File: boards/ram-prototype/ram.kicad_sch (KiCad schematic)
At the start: 48 parts, among them J1 SRAM_Bus, J2 DEC3_Unused, J3 Unused_COL_SEL, J4 DEC4_Unused

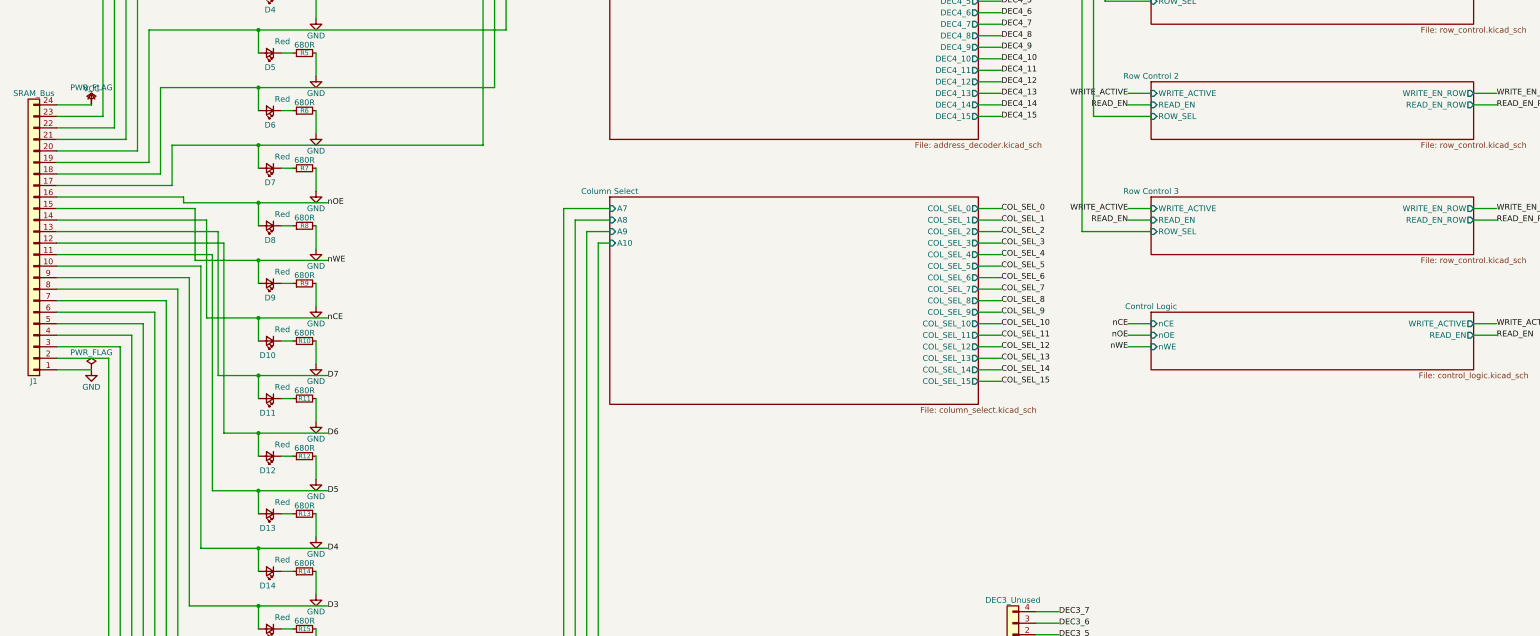
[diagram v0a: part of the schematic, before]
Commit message: add 8-pin PCIe power connector + TPS546D24A buck converter circuit
Adds on-board 12V→3.3V power supply to the RAM prototype using a
TPS546D24A 40A synchronous buck converter fed by an 8-pin PCIe
(Molex Mini-Fit Jr 2x4) connector. This establishes the power
architecture for all future boards (CPU, PPU).

New files:
- power_supply.kicad_sch: PCIe connector, buck converter, input/output
  filter caps, bootstrap/bypass caps, EN divider, PGOOD LED indicator
- shared/kicad-lib/symbols/Power_Discrete.kicad_sym: custom TPS546D24A
  symbol (41 pins at unique positions, placeholder footprint)

Infrastructure:
- symbols.py loads custom libs via CUSTOM_SYMBOL_LIBS in common.py
- schematic.py gains add_no_connect() and add_text() methods
- verify.py filters lib_symbol_issues as standalone artifact
- Library tables updated for Connector_Molex, Inductor_SMD, etc.

0 ERC errors, 0 verification warnings. 618 total BOM parts (+7).

Co-Authored-By: Claude Opus 4.6 (1M context) <noreply@anthropic.com>
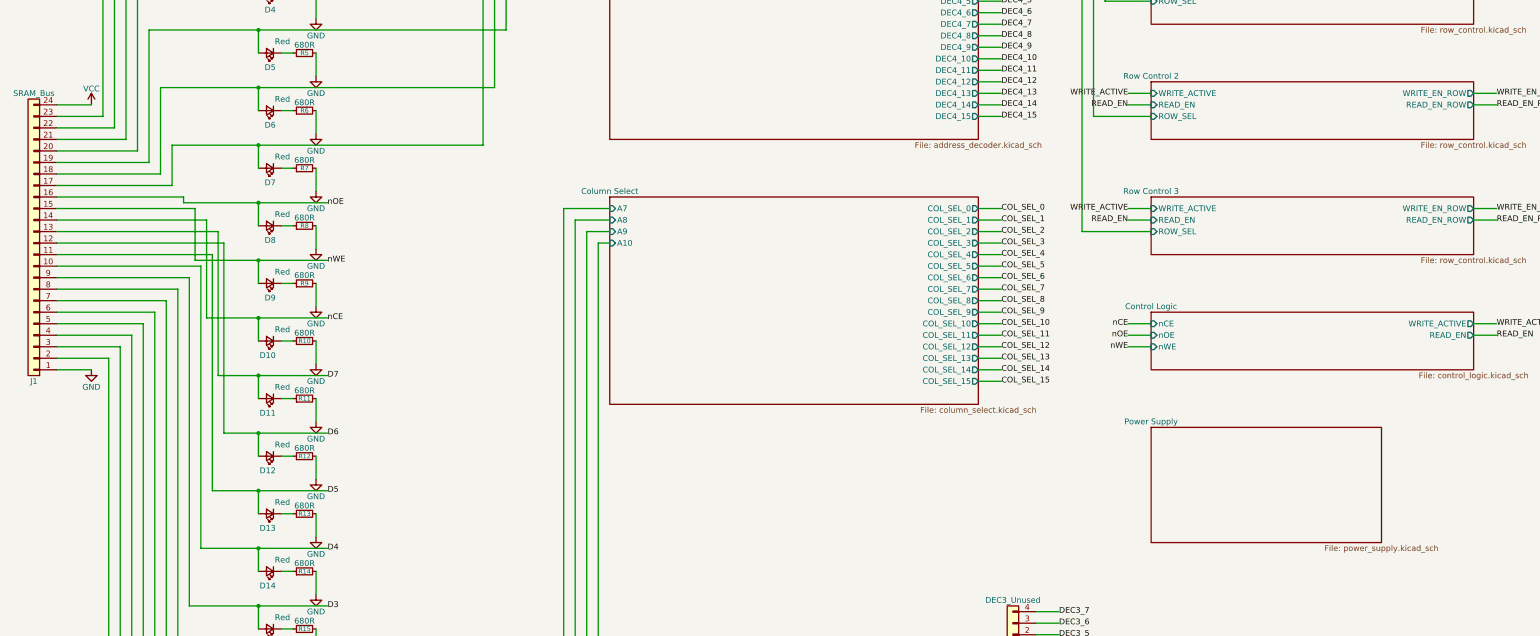
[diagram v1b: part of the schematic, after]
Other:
- added sheet Power Supply (power_supply.kicad_sch)

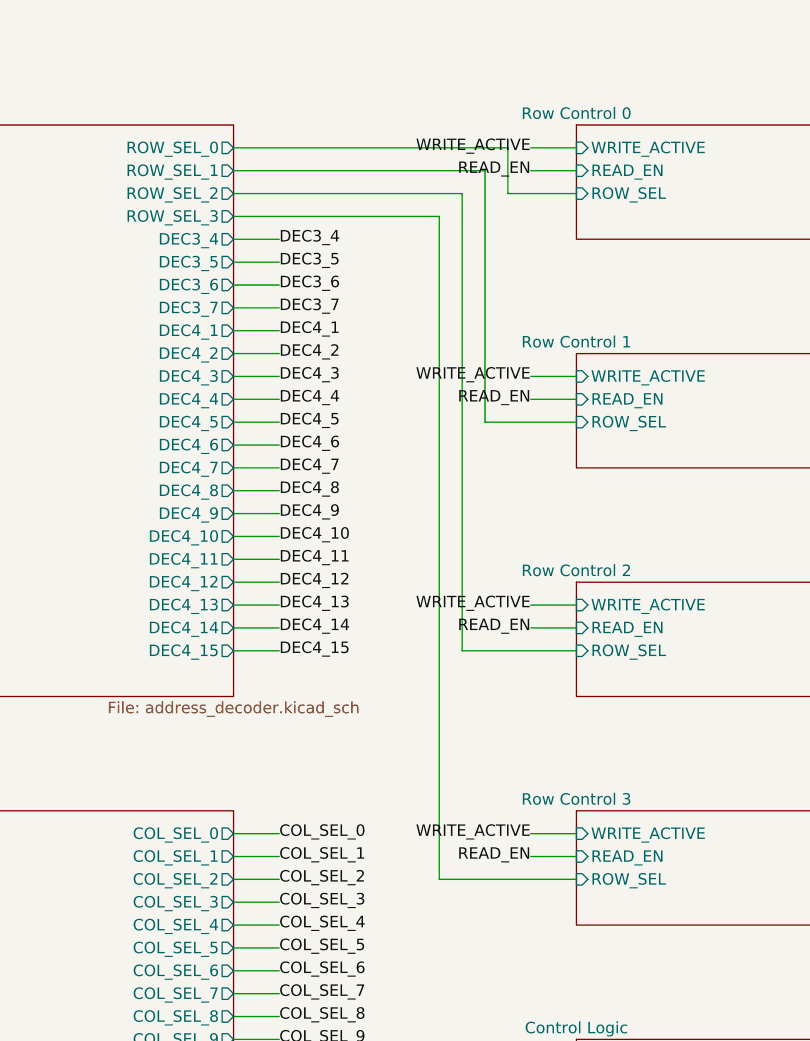
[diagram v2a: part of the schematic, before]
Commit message: add text overlap check to schematic verification and fix all violations
New check #12 in verify.py detects text overlapping wires, component
bodies, or other text. Smart exclusions for labels on their connection
wire and same-component Reference/Value pairs avoid false positives.

Fixes in generate_ram.py:
- Move ROW_SEL trunk wires from col2_x-3*GRID to col2_x-7*GRID so
  WRITE_ACTIVE/READ_EN labels don't overlap them
- Power supply: switch VDD5/BP1V5 bypass caps to angle=0 (vertical)
  with L-routes and 4*GRID vertical drop from IC pins
- Power supply: separate PGD L-route vertical X from pull-up resistor X
- Power supply: hide boot cap value (pin 2 wire unavoidably crosses it)

Co-Authored-By: Claude Opus 4.6 (1M context) <noreply@anthropic.com>
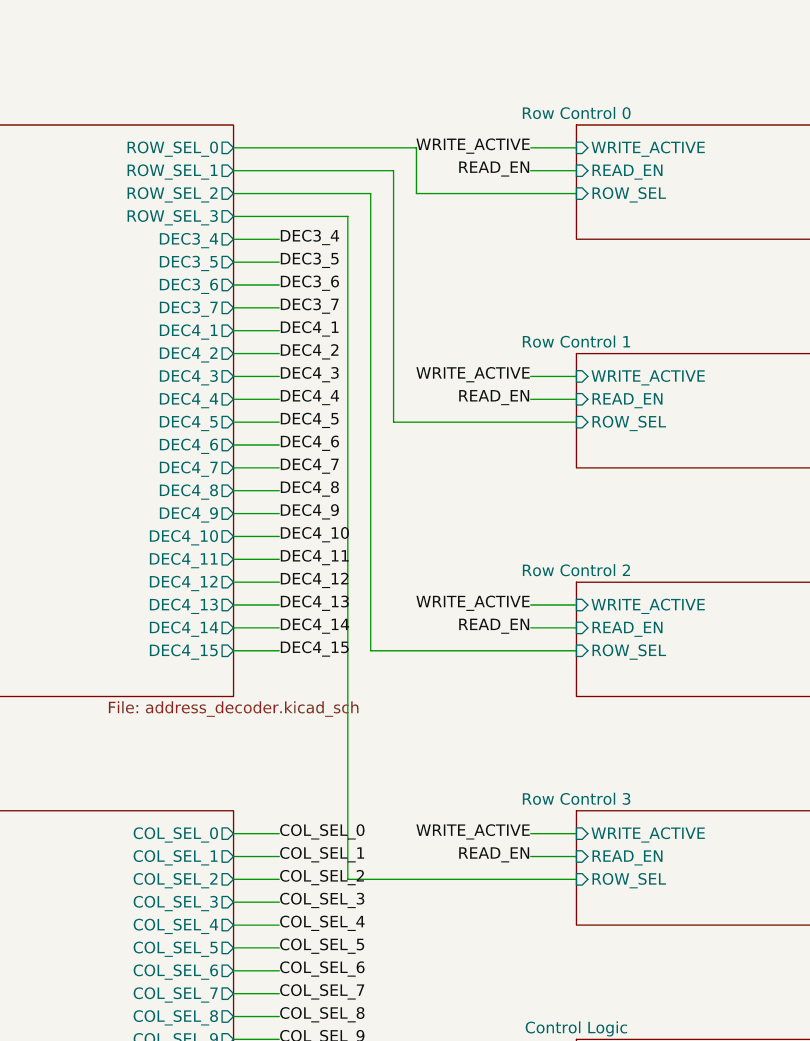
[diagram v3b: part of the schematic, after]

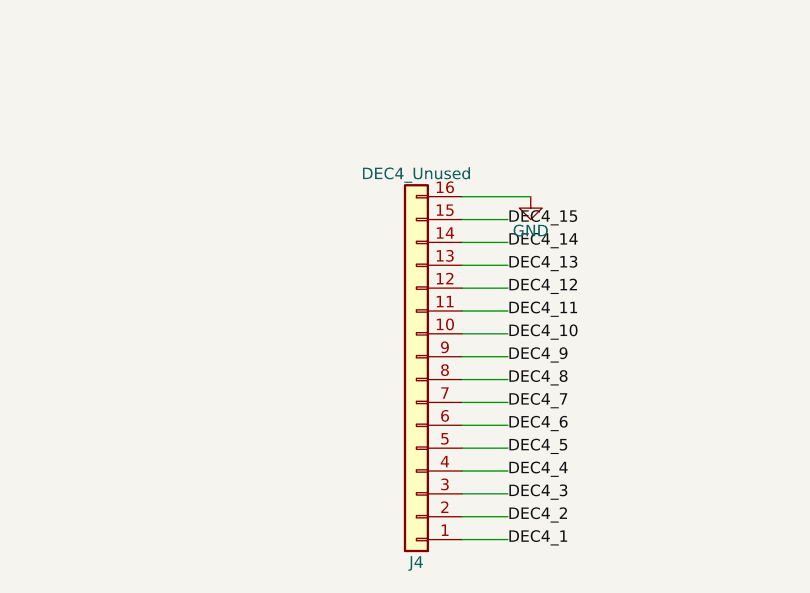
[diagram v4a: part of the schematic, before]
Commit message: replace J4 with 2-row connector and reposition J2/J4 headers
- Change J4 (DEC4 unused outputs) from Conn_01x16 to Conn_02x08_Odd_Even
  (2-row vertical pin header, more compact than 16-pin single row)
- Move J2 (DEC3) to top-left corner above main connector
- Move J4 (DEC4) to left of test grid, vertical orientation
- Add Conn_02x08_Odd_Even to symbol/footprint library maps
- Board size: 173 x 118 mm (down from 233 x 95 mm)
- 0 ERC errors/warnings, 0 DRC errors/warnings

Co-Authored-By: Claude Opus 4.6 (1M context) <noreply@anthropic.com>
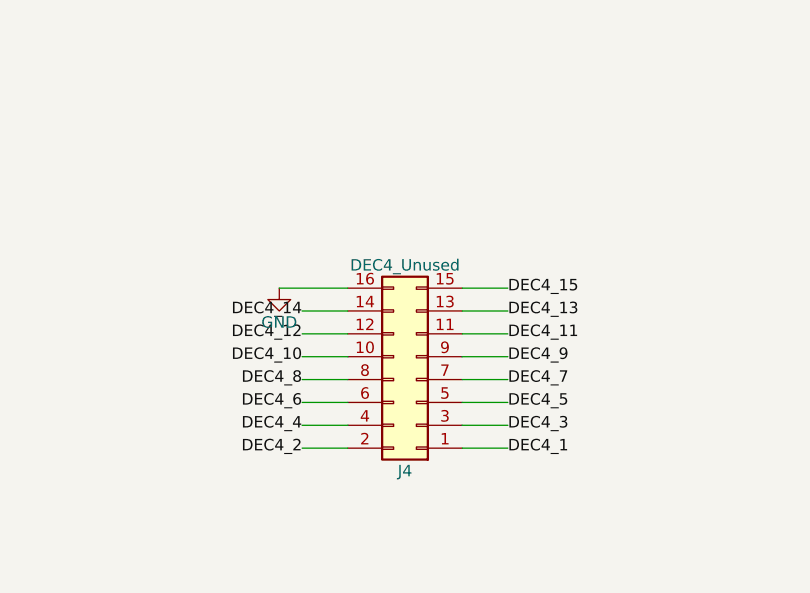
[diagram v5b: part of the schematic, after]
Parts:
- removed J4: DEC4_Unused, symbol Connector_Generic:Conn_01x16
- added J4: DEC4_Unused, symbol Connector_Generic:Conn_02x08_Odd_Even
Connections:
- net DEC4_1: now also J4.1 (Pin_1)
- net DEC4_10: now also J4.10 (Pin_10)
- net DEC4_11: now also J4.11 (Pin_11)
- net DEC4_12: now also J4.12 (Pin_12)
- net DEC4_13: now also J4.13 (Pin_13)
- net DEC4_14: now also J4.14 (Pin_14)
- net DEC4_15: now also J4.15 (Pin_15)
- net DEC4_2: now also J4.2 (Pin_2)
- net DEC4_3: now also J4.3 (Pin_3)
- net DEC4_4: now also J4.4 (Pin_4)
- net DEC4_5: now also J4.5 (Pin_5)
- net DEC4_6: now also J4.6 (Pin_6)
- net DEC4_7: now also J4.7 (Pin_7)
- net DEC4_8: now also J4.8 (Pin_8)
- net DEC4_9: now also J4.9 (Pin_9)
- net GND: now also J4.16 (Pin_16)

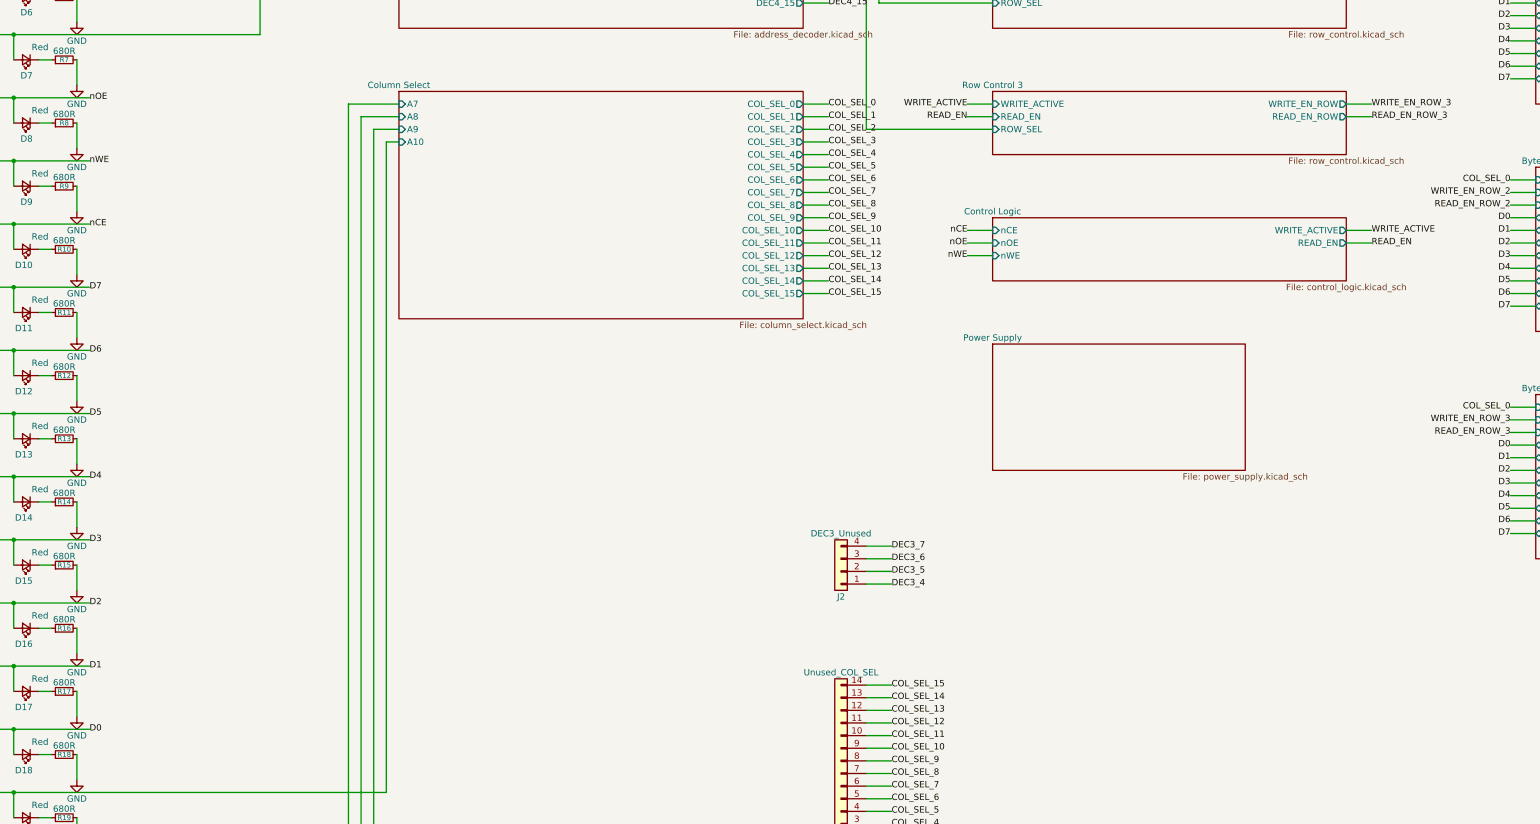
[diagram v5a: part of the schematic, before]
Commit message: swap D* and ctrl pins on connector, move ctrl logic below power supply
Data bus (D0-D7) now at pins 9-16, control (nCE/nWE/nOE) at pins 6-8.
Control Logic sheet block repositioned below Power Supply in col2.

Co-Authored-By: Claude Opus 4.6 (1M context) <noreply@anthropic.com>
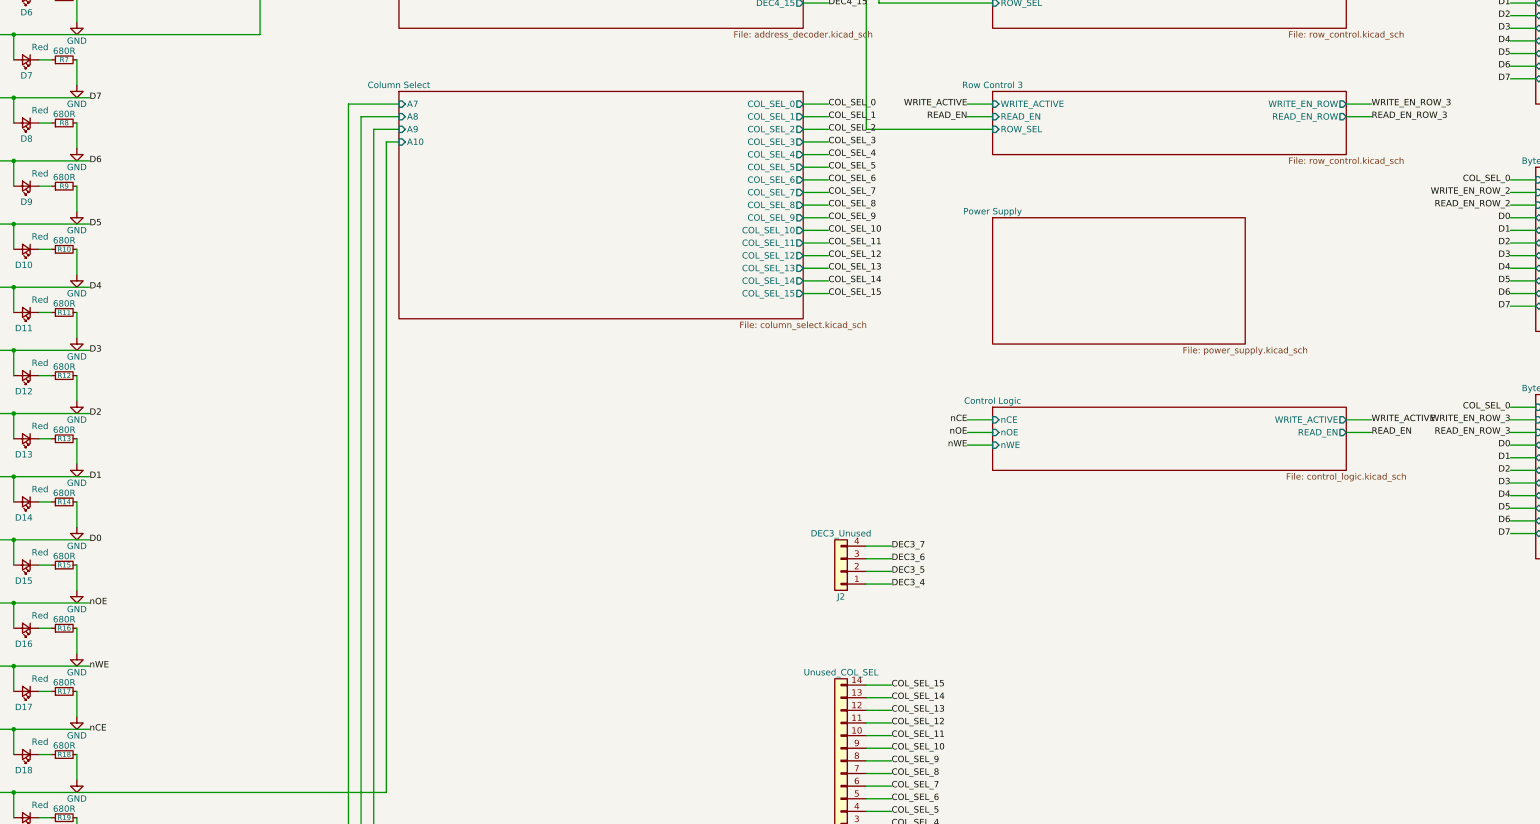
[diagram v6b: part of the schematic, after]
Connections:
- net D0: now also D15.2 (A), J1.9 (Pin_9); no longer D18.2 (A), J1.6 (Pin_6)
- net D1: now also D14.2 (A), J1.10 (Pin_10); no longer D17.2 (A), J1.7 (Pin_7)
- net D2: now also D13.2 (A), J1.11 (Pin_11); no longer D16.2 (A), J1.8 (Pin_8)
- net D3: now also D12.2 (A), J1.12 (Pin_12); no longer D15.2 (A), J1.9 (Pin_9)
- net D4: now also D11.2 (A), J1.13 (Pin_13); no longer D14.2 (A), J1.10 (Pin_10)
- net D5: now also D10.2 (A), J1.14 (Pin_14); no longer D13.2 (A), J1.11 (Pin_11)
- net D6: now also D9.2 (A), J1.15 (Pin_15); no longer D12.2 (A), J1.12 (Pin_12)
- net D7: now also D8.2 (A), J1.16 (Pin_16); no longer D11.2 (A), J1.13 (Pin_13)
- net nCE: now also D18.2 (A), J1.6 (Pin_6); no longer D10.2 (A), J1.14 (Pin_14)
- net nOE: now also D16.2 (A), J1.8 (Pin_8); no longer D8.2 (A), J1.16 (Pin_16)
- net nWE: now also D17.2 (A), J1.7 (Pin_7); no longer D9.2 (A), J1.15 (Pin_15)
